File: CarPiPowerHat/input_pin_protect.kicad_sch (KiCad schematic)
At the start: 4 parts

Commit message: Fixed some bugs, not done yet
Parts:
- added R29: 1M, Resistor_SMD:R_0603_1608Metric_Pad0.98x0.95mm_HandSolder, symbol Device:R
- C30: renamed from C23; value 10uF -> 22nF; LCSC C15850 -> (none)
- D3: renamed from D11; value TPGBLC12C -> PESD12VL1BA-N; LCSC C587149 -> C314261
- R22: renamed from R21; value 220 -> 10k; footprint Resistor_SMD:R_0402_1005Metric -> Resistor_SMD:R_0603_1608Metric_Pad0.98x0.95mm_HandSolder; LCSC C25091 -> (none)
- renumbered D9 to D7
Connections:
- net GND: now also R29.2
- net OUT: now also C30.1, D3.2 (A2), R22.1, R29.1
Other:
- moved on the sheet: R22
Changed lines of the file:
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@@
 (kicad_sch (version 20210621) (generator eeschema)
   (paper "A4")
+  (junction (at 120.65 80.01) (diameter 1.016) (color 0 0 0 0))
   (junction (at 129.54 80.01) (diameter 1.016) (color 0 0 0 0))
+  (junction (at 129.54 93.98) (diameter 1.016) (color 0 0 0 0))
   (junction (at 143.51 80.01) (diameter 1.016) (color 0 0 0 0))
   (junction (at 143.51 93.98) (diameter 1.016) (color 0 0 0 0))
-  (wire (pts (xy 104.14 80.01) (xy 118.11 80.01))
+  (junction (at 167.005 80.01) (diameter 1.016) (color 0 0 0 0))
+  (wire (pts (xy 104.14 80.01) (xy 109.22 80.01))
     (stroke (width 0) (type solid) (color 0 0 0 0))
   )
@@
     (stroke (width 0) (type solid) (color 0 0 0 0))
   )
-  (wire (pts (xy 125.73 80.01) (xy 129.54 80.01))
+  (wire (pts (xy 116.84 80.01) (xy 120.65 80.01))
+    (stroke (width 0) (type solid) (color 0 0 0 0))
+  )
+  (wire (pts (xy 120.65 80.01) (xy 120.65 82.55))
+    (stroke (width 0) (type solid) (color 0 0 0 0))
+  )
+  (wire (pts (xy 120.65 80.01) (xy 129.54 80.01))
+    (stroke (width 0) (type solid) (color 0 0 0 0))
+  )
+  (wire (pts (xy 120.65 90.17) (xy 120.65 93.98))
+    (stroke (width 0) (type solid) (color 0 0 0 0))
+  )
+  (wire (pts (xy 120.65 93.98) (xy 129.54 93.98))
     (stroke (width 0) (type solid) (color 0 0 0 0))
   )
@@
     (stroke (width 0) (type solid) (color 0 0 0 0))
   )
-  (wire (pts (xy 143.51 80.01) (xy 154.94 80.01))
+  (wire (pts (xy 143.51 71.12) (xy 167.005 71.12))
+    (stroke (width 0) (type solid) (color 0 0 0 0))
+  )
+  (wire (pts (xy 143.51 80.01) (xy 143.51 71.12))
     (stroke (width 0) (type solid) (color 0 0 0 0))
   )
@@
     (stroke (width 0) (type solid) (color 0 0 0 0))
   )
-  (wire (pts (xy 160.02 80.01) (xy 179.07 80.01))
+  (wire (pts (xy 160.02 80.01) (xy 167.005 80.01))
+    (stroke (width 0) (type solid) (color 0 0 0 0))
+  )
+  (wire (pts (xy 167.005 71.12) (xy 167.005 80.01))
+    (stroke (width 0) (type solid) (color 0 0 0 0))
+  )
+  (wire (pts (xy 167.005 80.01) (xy 179.07 80.01))
     (stroke (width 0) (type solid) (color 0 0 0 0))
   )
@@
     (effects (font (size 1.27 1.27)) (justify left))
   )
-  (symbol (lib_id "Device:R") (at 121.92 80.01 270)
+  (symbol (lib_id "Device:R") (at 113.03 80.01 270)
     (in_bom yes) (on_board yes)
-    (property "Reference" "R21" (id 0) (at 121.92 74.93 90))
-    (property "Value" "220" (id 1) (at 121.92 77.47 90))
-    (property "Footprint" "Resistor_SMD:R_0402_1005Metric" (id 2) (at 121.92 78.232 90)
+    (property "Reference" "R22" (id 0) (at 113.03 74.93 90))
+    (property "Value" "10k" (id 1) (at 113.03 77.47 90))
+    (property "Footprint" "Resistor_SMD:R_0603_1608Metric_Pad0.98x0.95mm_HandSolder" (id 2) (at 113.03 78.232 90)
       (effects (font (size 1.27 1.27)) hide)
     )
-    (property "Datasheet" "~" (id 3) (at 121.92 80.01 0)
+    (property "Datasheet" "~" (id 3) (at 113.03 80.01 0)
       (effects (font (size 1.27 1.27)) hide)
     )
-    (property "LCSC" "C25091" (id 4) (at 121.92 80.01 0)
+    (property "LCSC" "" (id 4) (at 113.03 80.01 0)
+      (effects (font (size 1.27 1.27)) hide)
+    )
+    (pin "1")
+    (pin "2")
+  )
+  (symbol (lib_id "Device:R") (at 120.65 86.36 0)
+    (in_bom yes) (on_board yes)
+    (property "Reference" "R29" (id 0) (at 115.57 86.36 90))
+    (property "Value" "1M" (id 1) (at 118.11 86.36 90))
+    (property "Footprint" "Resistor_SMD:R_0603_1608Metric_Pad0.98x0.95mm_HandSolder" (id 2) (at 118.872 86.36 90)
+      (effects (font (size 1.27 1.27)) hide)
+    )
+    (property "Datasheet" "~" (id 3) (at 120.65 86.36 0)
+      (effects (font (size 1.27 1.27)) hide)
+    )
+    (property "LCSC" "" (id 4) (at 120.65 86.36 0)
       (effects (font (size 1.27 1.27)) hide)
     )
@@
   (symbol (lib_id "Device:D_TVS") (at 143.51 86.36 90)
     (in_bom yes) (on_board yes)
-    (property "Reference" "D11" (id 0) (at 146.05 85.09 90)
+    (property "Reference" "D3" (id 0) (at 146.05 85.09 90)
       (effects (font (size 1.27 1.27)) (justify right))
     )
-    (property "Value" "TPGBLC12C" (id 1) (at 146.05 87.63 90)
+    (property "Value" "PESD12VL1BA-N" (id 1) (at 146.05 87.63 90)
       (effects (font (size 1.27 1.27)) (justify right))
     )
@@
       (effects (font (size 1.27 1.27)) hide)
     )
-    (property "LCSC" "C587149" (id 4) (at 143.51 86.36 90)
+    (property "LCSC" "C314261" (id 4) (at 143.51 86.36 90)
       (effects (font (size 1.27 1.27)) hide)
     )
@@
   (symbol (lib_id "Device:C") (at 129.54 86.36 0)
     (in_bom yes) (on_board yes)
-    (property "Reference" "C23" (id 0) (at 133.985 85.09 0)
+    (property "Reference" "C30" (id 0) (at 133.985 85.09 0)
       (effects (font (size 1.27 1.27)) (justify left))
     )
-    (property "Value" "10uF" (id 1) (at 133.985 87.63 0)
+    (property "Value" "22nF" (id 1) (at 133.985 87.63 0)
       (effects (font (size 1.27 1.27)) (justify left))
     )
@@
       (effects (font (size 1.27 1.27)) hide)
     )
-    (property "LCSC" "C15850" (id 6) (at 129.54 86.36 0)
+    (property "LCSC" "" (id 6) (at 129.54 86.36 0)
       (effects (font (size 1.27 1.27)) hide)
     )
@@
   (symbol (lib_id "Diode:BAT54S") (at 154.94 80.01 90)
     (in_bom yes) (on_board yes)
-    (property "Reference" "D9" (id 0) (at 163.83 78.7399 90)
+    (property "Reference" "D7" (id 0) (at 163.83 78.7399 90)
       (effects (font (size 1.27 1.27)) (justify left))
     )

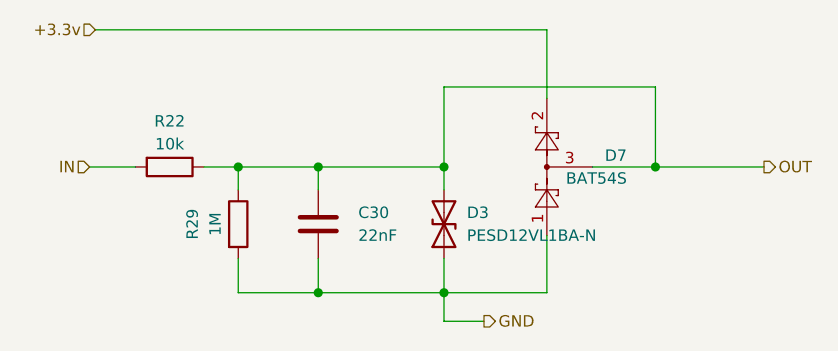
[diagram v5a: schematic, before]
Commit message: removed unnecessary reverse polarity protection
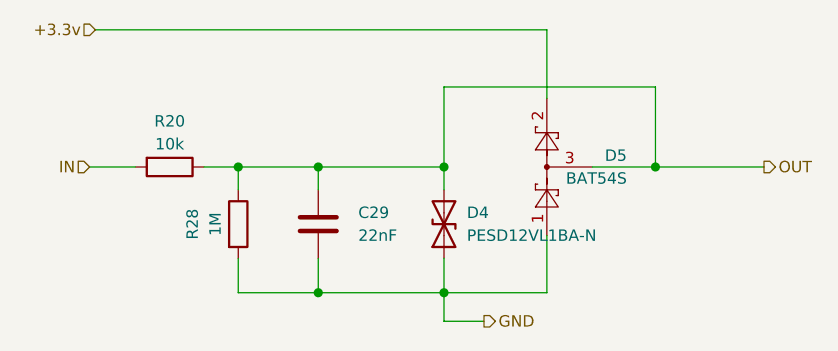
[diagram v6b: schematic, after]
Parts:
- renumbered C30 to C29, D3 to D4, D7 to D5, R22 to R20, R29 to R28
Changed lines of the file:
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@@
   (symbol (lib_id "Device:R") (at 113.03 80.01 270)
     (in_bom yes) (on_board yes)
-    (property "Reference" "R22" (id 0) (at 113.03 74.93 90))
+    (property "Reference" "R20" (id 0) (at 113.03 74.93 90))
     (property "Value" "10k" (id 1) (at 113.03 77.47 90))
     (property "Footprint" "Resistor_SMD:R_0603_1608Metric_Pad0.98x0.95mm_HandSolder" (id 2) (at 113.03 78.232 90)
@@
   (symbol (lib_id "Device:R") (at 120.65 86.36 0)
     (in_bom yes) (on_board yes)
-    (property "Reference" "R29" (id 0) (at 115.57 86.36 90))
+    (property "Reference" "R28" (id 0) (at 115.57 86.36 90))
     (property "Value" "1M" (id 1) (at 118.11 86.36 90))
     (property "Footprint" "Resistor_SMD:R_0603_1608Metric_Pad0.98x0.95mm_HandSolder" (id 2) (at 118.872 86.36 90)
@@
   (symbol (lib_id "Device:D_TVS") (at 143.51 86.36 90)
     (in_bom yes) (on_board yes)
-    (property "Reference" "D3" (id 0) (at 146.05 85.09 90)
+    (property "Reference" "D4" (id 0) (at 146.05 85.09 90)
       (effects (font (size 1.27 1.27)) (justify right))
     )
@@
   (symbol (lib_id "Device:C") (at 129.54 86.36 0)
     (in_bom yes) (on_board yes)
-    (property "Reference" "C30" (id 0) (at 133.985 85.09 0)
+    (property "Reference" "C29" (id 0) (at 133.985 85.09 0)
       (effects (font (size 1.27 1.27)) (justify left))
     )
@@
   (symbol (lib_id "Diode:BAT54S") (at 154.94 80.01 90)
     (in_bom yes) (on_board yes)
-    (property "Reference" "D7" (id 0) (at 163.83 78.7399 90)
+    (property "Reference" "D5" (id 0) (at 163.83 78.7399 90)
       (effects (font (size 1.27 1.27)) (justify left))
     )

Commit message: Finalized 2.2
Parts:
- C30: renamed from C29; LCSC (none) -> C1729
- R22: renamed from R20; LCSC (none) -> C25804
- R29: renamed from R28; LCSC (none) -> C22935
- renumbered D4 to D3, D5 to D7
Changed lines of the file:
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@@
   (symbol (lib_id "Device:R") (at 113.03 80.01 270)
     (in_bom yes) (on_board yes)
-    (property "Reference" "R20" (id 0) (at 113.03 74.93 90))
+    (property "Reference" "R22" (id 0) (at 113.03 74.93 90))
     (property "Value" "10k" (id 1) (at 113.03 77.47 90))
     (property "Footprint" "Resistor_SMD:R_0603_1608Metric_Pad0.98x0.95mm_HandSolder" (id 2) (at 113.03 78.232 90)
@@
       (effects (font (size 1.27 1.27)) hide)
     )
-    (property "LCSC" "" (id 4) (at 113.03 80.01 0)
+    (property "LCSC" "C25804" (id 4) (at 113.03 80.01 0)
       (effects (font (size 1.27 1.27)) hide)
     )
@@
   (symbol (lib_id "Device:R") (at 120.65 86.36 0)
     (in_bom yes) (on_board yes)
-    (property "Reference" "R28" (id 0) (at 115.57 86.36 90))
+    (property "Reference" "R29" (id 0) (at 115.57 86.36 90))
     (property "Value" "1M" (id 1) (at 118.11 86.36 90))
     (property "Footprint" "Resistor_SMD:R_0603_1608Metric_Pad0.98x0.95mm_HandSolder" (id 2) (at 118.872 86.36 90)
@@
       (effects (font (size 1.27 1.27)) hide)
     )
-    (property "LCSC" "" (id 4) (at 120.65 86.36 0)
+    (property "LCSC" "C22935" (id 4) (at 120.65 86.36 0)
       (effects (font (size 1.27 1.27)) hide)
     )
@@
   (symbol (lib_id "Device:D_TVS") (at 143.51 86.36 90)
     (in_bom yes) (on_board yes)
-    (property "Reference" "D4" (id 0) (at 146.05 85.09 90)
+    (property "Reference" "D3" (id 0) (at 146.05 85.09 90)
       (effects (font (size 1.27 1.27)) (justify right))
     )
@@
   (symbol (lib_id "Device:C") (at 129.54 86.36 0)
     (in_bom yes) (on_board yes)
-    (property "Reference" "C29" (id 0) (at 133.985 85.09 0)
+    (property "Reference" "C30" (id 0) (at 133.985 85.09 0)
       (effects (font (size 1.27 1.27)) (justify left))
     )
@@
       (effects (font (size 1.27 1.27)) hide)
     )
-    (property "LCSC" "" (id 6) (at 129.54 86.36 0)
+    (property "LCSC" "C1729" (id 6) (at 129.54 86.36 0)
       (effects (font (size 1.27 1.27)) hide)
     )
@@
   (symbol (lib_id "Diode:BAT54S") (at 154.94 80.01 90)
     (in_bom yes) (on_board yes)
-    (property "Reference" "D5" (id 0) (at 163.83 78.7399 90)
+    (property "Reference" "D7" (id 0) (at 163.83 78.7399 90)
       (effects (font (size 1.27 1.27)) (justify left))
     )

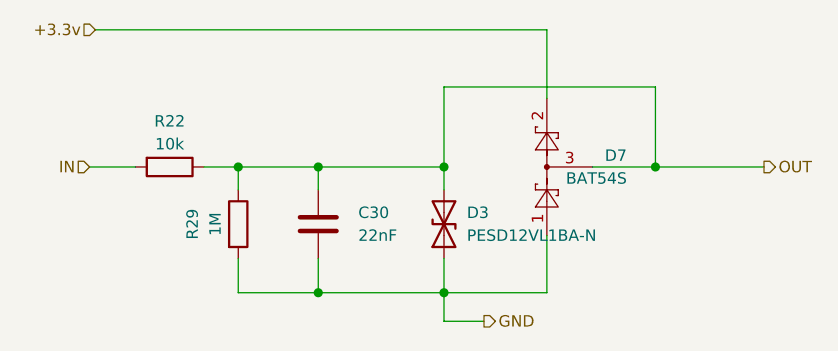
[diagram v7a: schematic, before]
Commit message: Finalizing, checking parts
Might be ready for production
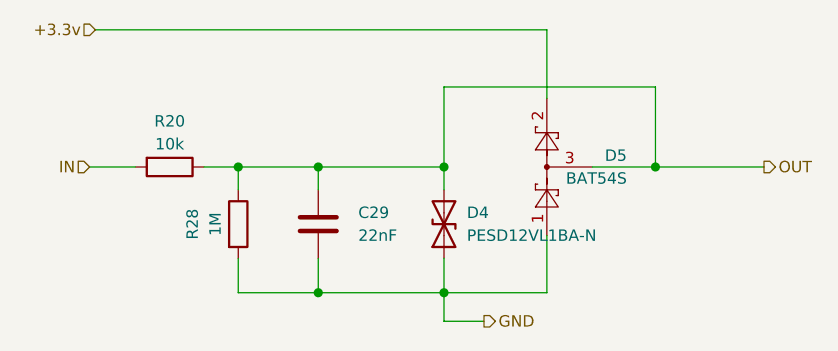
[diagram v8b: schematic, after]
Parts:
- R20: renamed from R22; footprint Resistor_SMD:R_0603_1608Metric_Pad0.98x0.95mm_HandSolder -> Resistor_SMD:R_0805_2012Metric_Pad1.20x1.40mm_HandSolder; LCSC C25804 -> C17414
- R28: renamed from R29; footprint Resistor_SMD:R_0603_1608Metric_Pad0.98x0.95mm_HandSolder -> Resistor_SMD:R_0805_2012Metric_Pad1.20x1.40mm_HandSolder; LCSC C22935 -> C17514
- renumbered C30 to C29, D3 to D4, D7 to D5
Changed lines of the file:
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@@
   (symbol (lib_id "Device:R") (at 113.03 80.01 270)
     (in_bom yes) (on_board yes)
-    (property "Reference" "R22" (id 0) (at 113.03 74.93 90))
+    (property "Reference" "R20" (id 0) (at 113.03 74.93 90))
     (property "Value" "10k" (id 1) (at 113.03 77.47 90))
-    (property "Footprint" "Resistor_SMD:R_0603_1608Metric_Pad0.98x0.95mm_HandSolder" (id 2) (at 113.03 78.232 90)
+    (property "Footprint" "Resistor_SMD:R_0805_2012Metric_Pad1.20x1.40mm_HandSolder" (id 2) (at 113.03 78.232 90)
       (effects (font (size 1.27 1.27)) hide)
     )
@@
       (effects (font (size 1.27 1.27)) hide)
     )
-    (property "LCSC" "C25804" (id 4) (at 113.03 80.01 0)
+    (property "LCSC" "C17414" (id 4) (at 113.03 80.01 0)
       (effects (font (size 1.27 1.27)) hide)
     )
@@
   (symbol (lib_id "Device:R") (at 120.65 86.36 0)
     (in_bom yes) (on_board yes)
-    (property "Reference" "R29" (id 0) (at 115.57 86.36 90))
+    (property "Reference" "R28" (id 0) (at 115.57 86.36 90))
     (property "Value" "1M" (id 1) (at 118.11 86.36 90))
-    (property "Footprint" "Resistor_SMD:R_0603_1608Metric_Pad0.98x0.95mm_HandSolder" (id 2) (at 118.872 86.36 90)
+    (property "Footprint" "Resistor_SMD:R_0805_2012Metric_Pad1.20x1.40mm_HandSolder" (id 2) (at 118.872 86.36 90)
       (effects (font (size 1.27 1.27)) hide)
     )
@@
       (effects (font (size 1.27 1.27)) hide)
     )
-    (property "LCSC" "C22935" (id 4) (at 120.65 86.36 0)
+    (property "LCSC" "C17514" (id 4) (at 120.65 86.36 0)
       (effects (font (size 1.27 1.27)) hide)
     )
@@
   (symbol (lib_id "Device:D_TVS") (at 143.51 86.36 90)
     (in_bom yes) (on_board yes)
-    (property "Reference" "D3" (id 0) (at 146.05 85.09 90)
+    (property "Reference" "D4" (id 0) (at 146.05 85.09 90)
       (effects (font (size 1.27 1.27)) (justify right))
     )
@@
   (symbol (lib_id "Device:C") (at 129.54 86.36 0)
     (in_bom yes) (on_board yes)
-    (property "Reference" "C30" (id 0) (at 133.985 85.09 0)
+    (property "Reference" "C29" (id 0) (at 133.985 85.09 0)
       (effects (font (size 1.27 1.27)) (justify left))
     )
@@
   (symbol (lib_id "Diode:BAT54S") (at 154.94 80.01 90)
     (in_bom yes) (on_board yes)
-    (property "Reference" "D7" (id 0) (at 163.83 78.7399 90)
+    (property "Reference" "D5" (id 0) (at 163.83 78.7399 90)
       (effects (font (size 1.27 1.27)) (justify left))
     )
